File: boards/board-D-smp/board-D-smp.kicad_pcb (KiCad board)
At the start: 4 copper layers, 73.7 x 112 mm, 30 parts, among them J5 SAMTEC_QSE-040-01-X-D-A, K0 SMP_Amphenol_SMP-MSSB-PCS_Ver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, K1 SMP_Amphenol_SMP-MSSB-PCS_Ver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, K10 SMP_Amphenol_SMP-MSSB-PCS_Ver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, K11 SMP_Amphenol_SMP-MSSB-PCS_Ver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, K12 SMP_Amphenol_SMP-MSSB-PCS_Ver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, K13 SMP_Amphenol_SMP-MSSB-PCS_Ver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, K14 SMP_Amphenol_SMP-MSSB-PCS_Ver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, K15 SMP_Amphenol_SMP-MSSB-PCS_Ver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, K16 SMP_Amphenol_SMP-MSSB-PCS_Ver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, K17 SMP_Amphenol_SMP-MSSB-PCS_Ver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, K18 SMP_Amphenol_SMP-MSSB-PCS_Ver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, K19 SMP_Amphenol_SMP-MSSB-PCS_Ver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, K2 SMP_Amphenol_SMP-MSSB-PCS_Ver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, K20 SMP_Amphenol_SMP-MSSB-PCS_Ver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, K21 SMP_Amphenol_SMP-MSSB-PCS_Ver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, K22 SMP_Amphenol_SMP-MSSB-PCS_Ver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, K23 SMP_Amphenol_SMP-MSSB-PCS_Ver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, K3 SMP_Amphenol_SMP-MSSB-PCS_Ver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, K4 SMP_Amphenol_SMP-MSSB-PCS_Ver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, K5 SMP_Amphenol_SMP-MSSB-PCS_Ver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, K6 SMP_Amphenol_SMP-MSSB-PCS_Ver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, K7 SMP_Amphenol_SMP-MSSB-PCS_Ver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, K8 SMP_Amphenol_SMP-MSSB-PCS_Ver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, K9 SMP_Amphenol_SMP-MSSB-PCS_Ver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

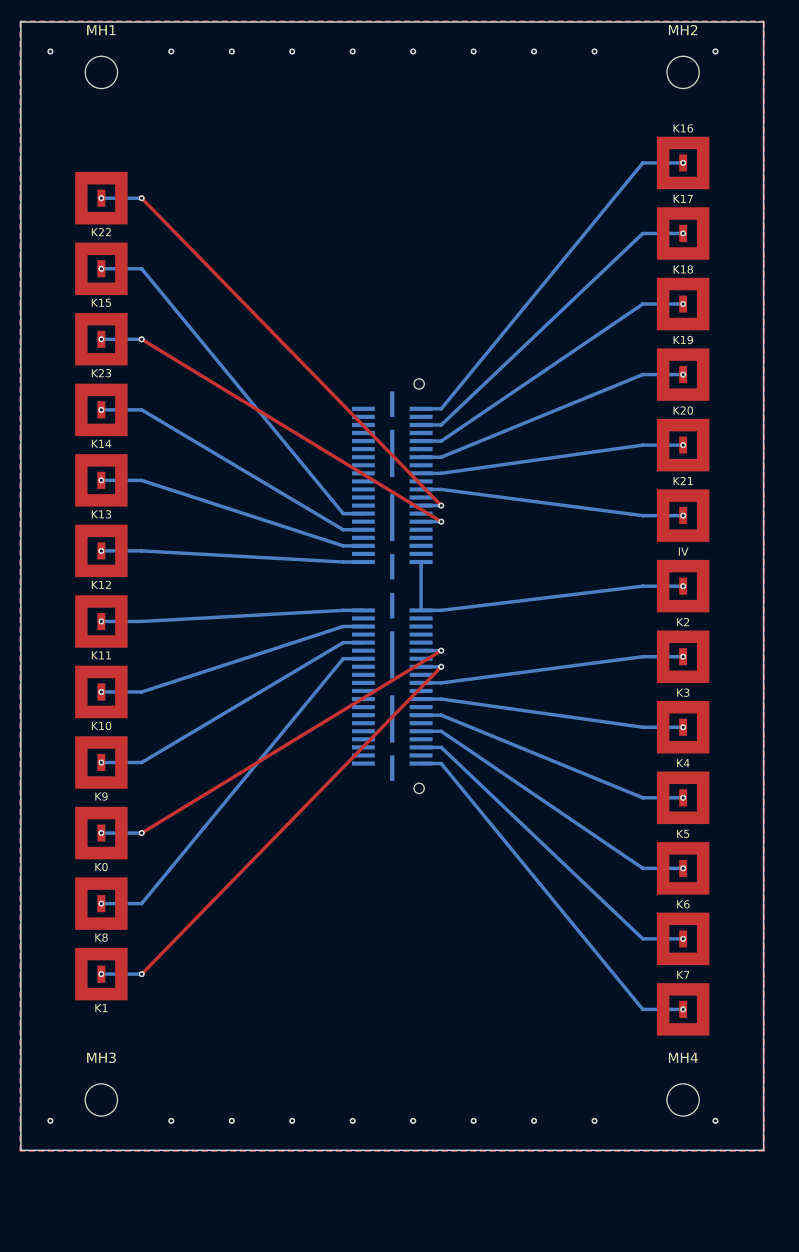
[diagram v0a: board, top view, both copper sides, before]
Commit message: Add SMP Board D, mount J5 on back face, collect CAD assets + master BOM
Boards / generator:
- New Board D (SMP): Amphenol SMP-MSLD-PCS-20 vertical SMT jack; external signal
  tab routes like the other flat SMD jacks (no via-in-pad).
- Mount J5 (QSE-040) on the back PCB face on all boards (detector plugs into the
  back, jacks on the front); finalize_board.py routes escapes on the QSE's actual
  copper layer, hopping layers only for the crossing fans.
- Board A switched to straight surface-mount MCX (MCX-J-P-X-ST-SM1).
- _edge auto-rotates every flat/vertical jack so its signal pad faces the QSE,
  derived from the part's real pad geometry (U.FL/MCX/SMP).
- All four boards regenerated: DRC 0/0, 0 unconnected; fab packages + BOMs re-exported.

CAD asset collection:
- Datasheets for all 5 parts in docs/datasheets/ (Samtec QSE + MCX, Amphenol SMA +
  SMP, Hirose U.FL).
- Consolidated schematic-symbol library lib/ets-breakout.kicad_sym (reference-only;
  boards are built from pinout.py).
- Local 3D STEP models for QSE, MCX, U.FL, SMP (SMA 3D is vendor-gated - documented).
- Master BOM + CAD-asset matrix: docs/BOM.md, docs/BOM.csv.

Housekeeping:
- Removed temp import files captured by the prior commit (_tmp_smp20/, root drop-ins);
  ignore _tmp*/ and _stage*/ going forward.

Co-Authored-By: Claude Opus 4.8 <noreply@anthropic.com>
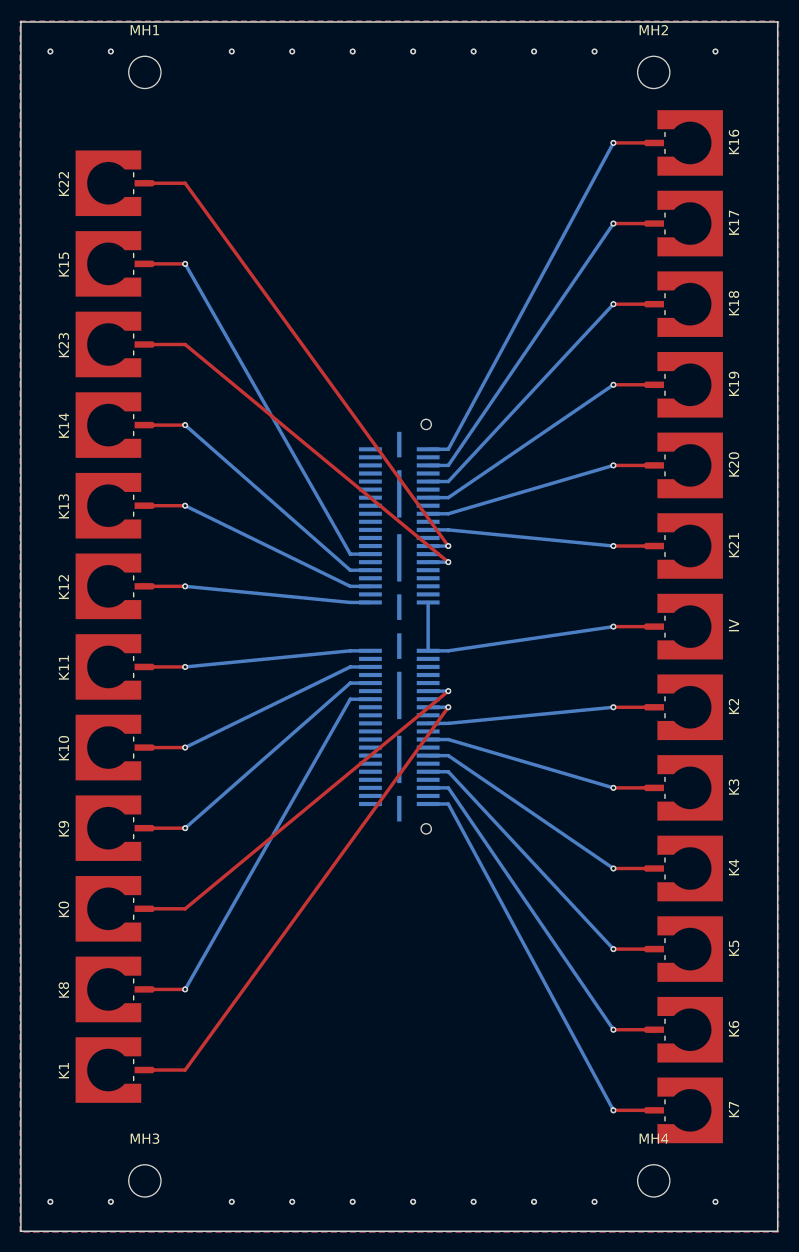
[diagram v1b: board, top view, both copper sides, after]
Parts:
- removed the IV at (74.7, 66.0)
- added IV: SMP_Amphenol_SMP-MSLD-PCS-20, SMP_Amphenol_SMP-MSLD-PCS-20, F.Cu at (75.4, 70.0)
- K0, K1, K10, K11, K12, K13, K14, K15, K16, K17, K18, K19, K2, K20, K21, K22, K23, K3, K4, K5, K6, K7, K8, K9: value SMP_Amphenol_SMP-MSSB-PCS_Vertical -> SMP_Amphenol_SMP-MSLD-PCS-20; footprint SMP_Amphenol_SMP-MSSB-PCS_Vertical -> SMP_Amphenol_SMP-MSLD-PCS-20
- moved K7 10.0 mm to (75.4, 118.0), turned to -90 degrees
- moved K1 9.54 mm to (17.7, 114.0), turned to 90 degrees
- moved MH3 9.12 mm to (21.3, 125.0)
- moved K6 9.04 mm to (75.4, 110.0), turned to -90 degrees
- moved K8 8.54 mm to (17.7, 106.0), turned to 90 degrees
- moved MH4 8.54 mm to (71.8, 125.0)
- moved K5 8.05 mm to (75.4, 102.0), turned to -90 degrees
- moved K0 7.55 mm to (17.7, 98.0), turned to 90 degrees
- moved K4 7.05 mm to (75.4, 94.0), turned to -90 degrees
- moved K9 6.55 mm to (17.7, 90.0), turned to 90 degrees
- moved K3 6.06 mm to (75.4, 86.0), turned to -90 degrees
- moved K10 5.56 mm to (17.7, 82.0), turned to 90 degrees
- moved K2 5.06 mm to (75.4, 78.0), turned to -90 degrees
- moved K11 4.57 mm to (17.7, 74.0), turned to 90 degrees
- moved MH1 4.32 mm to (21.3, 15.0)
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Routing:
- net SIPM_K21: track 26.2 -> 22.5 mm
- net SIPM_K2: track 26.2 -> 22.5 mm
- net IV: track 30.9 -> 27.4 mm
- net SIPM_K12: track 26.0 -> 22.5 mm
- net SIPM_K11: track 26.0 -> 22.5 mm
- net SIPM_K3: track 26.2 -> 23.1 mm
- net SIPM_K20: track 26.2 -> 23.1 mm
- net SIPM_K7: track 37.5 -> 40.5 mm
- net SIPM_K16: track 37.5 -> 40.5 mm
- net SIPM_K13: track 27.0 -> 24.2 mm
- net SIPM_K10: track 27.0 -> 24.2 mm
- net SIPM_K22: track 48.6 -> 50.5 mm, vias 3 -> 1
- net SIPM_K1: track 48.6 -> 50.5 mm, vias 3 -> 1
- net SIPM_K4: track 27.6 -> 25.8 mm
- net SIPM_K19: track 27.6 -> 25.8 mm
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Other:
- board size 73.7 x 112 mm -> 75.1 x 120 mm
